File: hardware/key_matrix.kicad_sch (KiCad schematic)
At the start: 90 parts, among them SW10 SW_SPST, SW11 SW_SPST, SW12 SW_SPST, SW13 SW_SPST, SW14 SW_SPST, SW15 SW_SPST, SW16 SW_SPST, SW17 SW_SPST, SW18 SW_SPST, SW19 SW_SPST, SW2 SW_SPST, SW20 SW_SPST, SW21 SW_SPST, SW22 SW_SPST, SW23 SW_SPST, SW24 SW_SPST, SW25 SW_SPST, SW26 SW_SPST, SW27 SW_SPST, SW28 SW_SPST, SW29 SW_SPST, SW3 SW_SPST, SW30 SW_SPST, SW31 SW_SPST, SW32 SW_SPST, SW33 SW_SPST, SW34 SW_SPST, SW35 SW_SPST, SW36 SW_SPST, SW37 SW_SPST, SW38 SW_SPST, SW39 SW_SPST, SW4 SW_SPST, SW40 SW_SPST, SW41 SW_SPST, SW42 SW_SPST, SW43 SW_SPST, SW44 SW_SPST, SW45 SW_SPST, SW46 SW_SPST, SW47 SW_SPST, SW48 SW_SPST, SW49 SW_SPST, SW5 SW_SPST, SW50 SW_SPST, SW51 SW_SPST, SW52 SW_SPST, SW53 SW_SPST, SW54 SW_SPST, SW55 SW_SPST, SW56 SW_SPST, SW57 SW_SPST, SW58 SW_SPST, SW59 SW_SPST, SW6 SW_SPST, SW60 SW_SPST, SW61 SW_SPST, SW62 SW_SPST, SW63 SW_SPST, SW64 SW_SPST, SW65 SW_SPST, SW66 SW_SPST, SW67 SW_SPST, SW68 SW_SPST, SW69 SW_SPST, SW7 SW_SPST, SW70 SW_SPST, SW71 SW_SPST, SW72 SW_SPST, SW73 SW_SPST, SW75 SW_SPST, SW76 SW_SPST, SW77 SW_SPST, SW78 SW_SPST, SW79 SW_SPST, SW8 SW_SPST, SW80 SW_SPST, SW81 SW_SPST, SW82 SW_SPST, SW9 SW_SPST

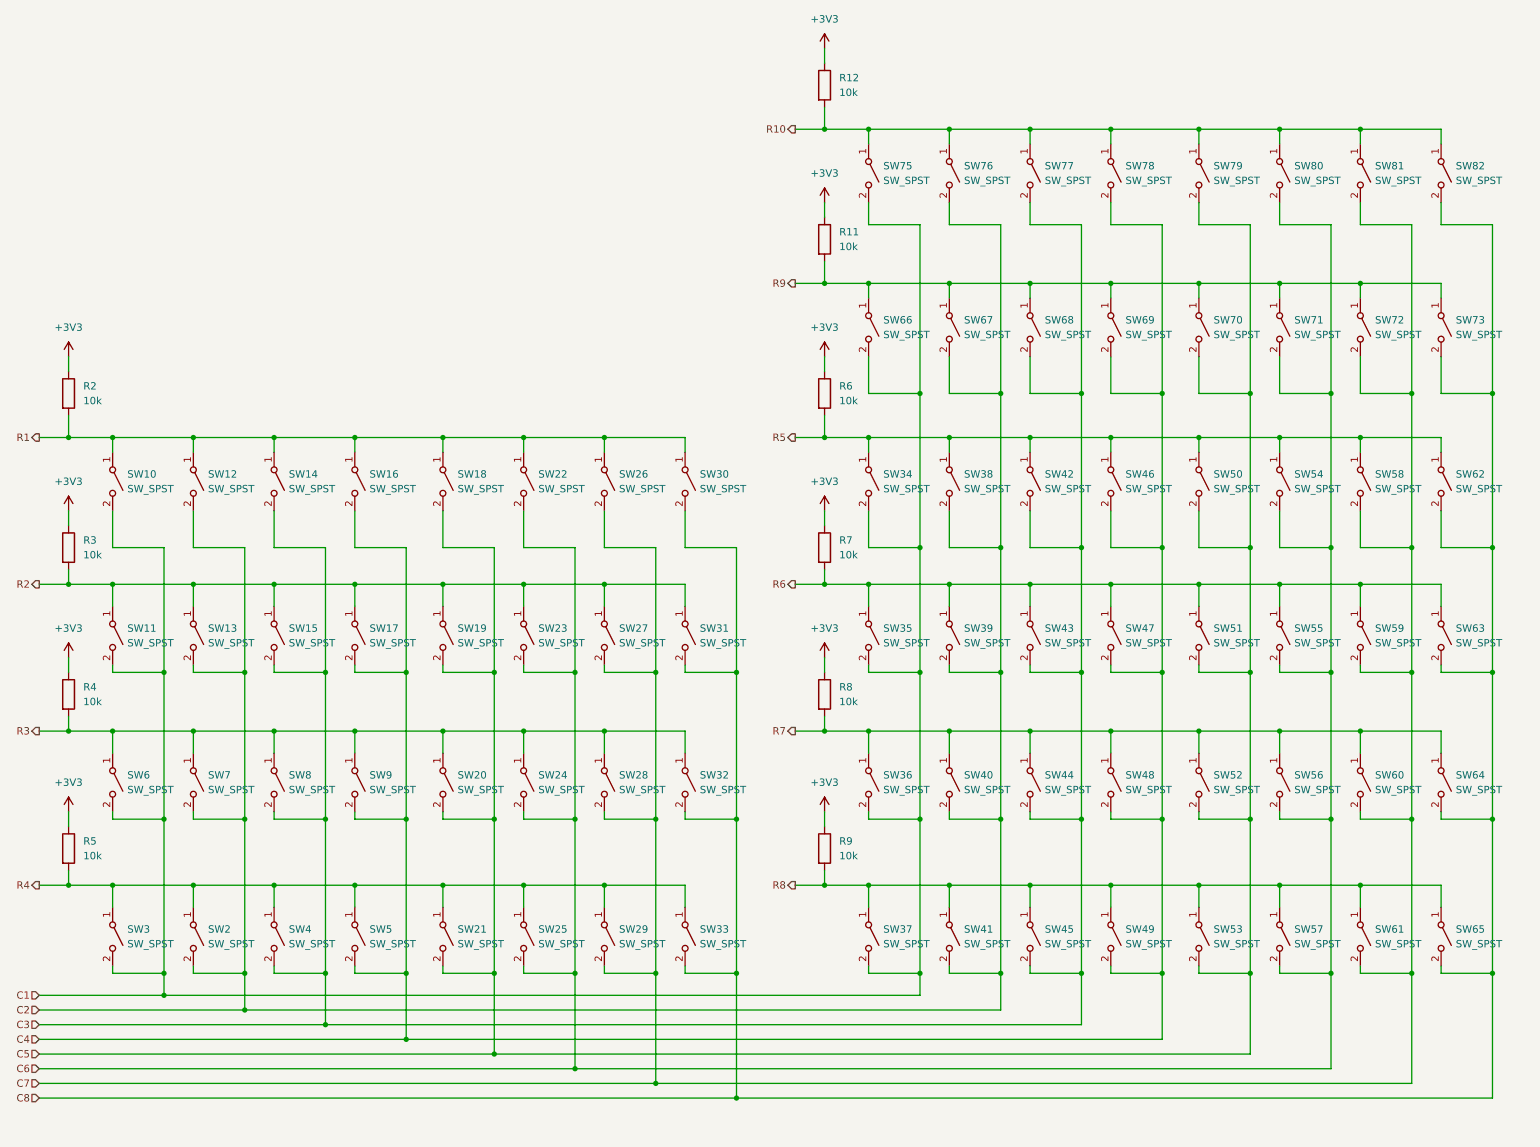
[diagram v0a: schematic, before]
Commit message: Add diodes to schematic to prevent ghosting
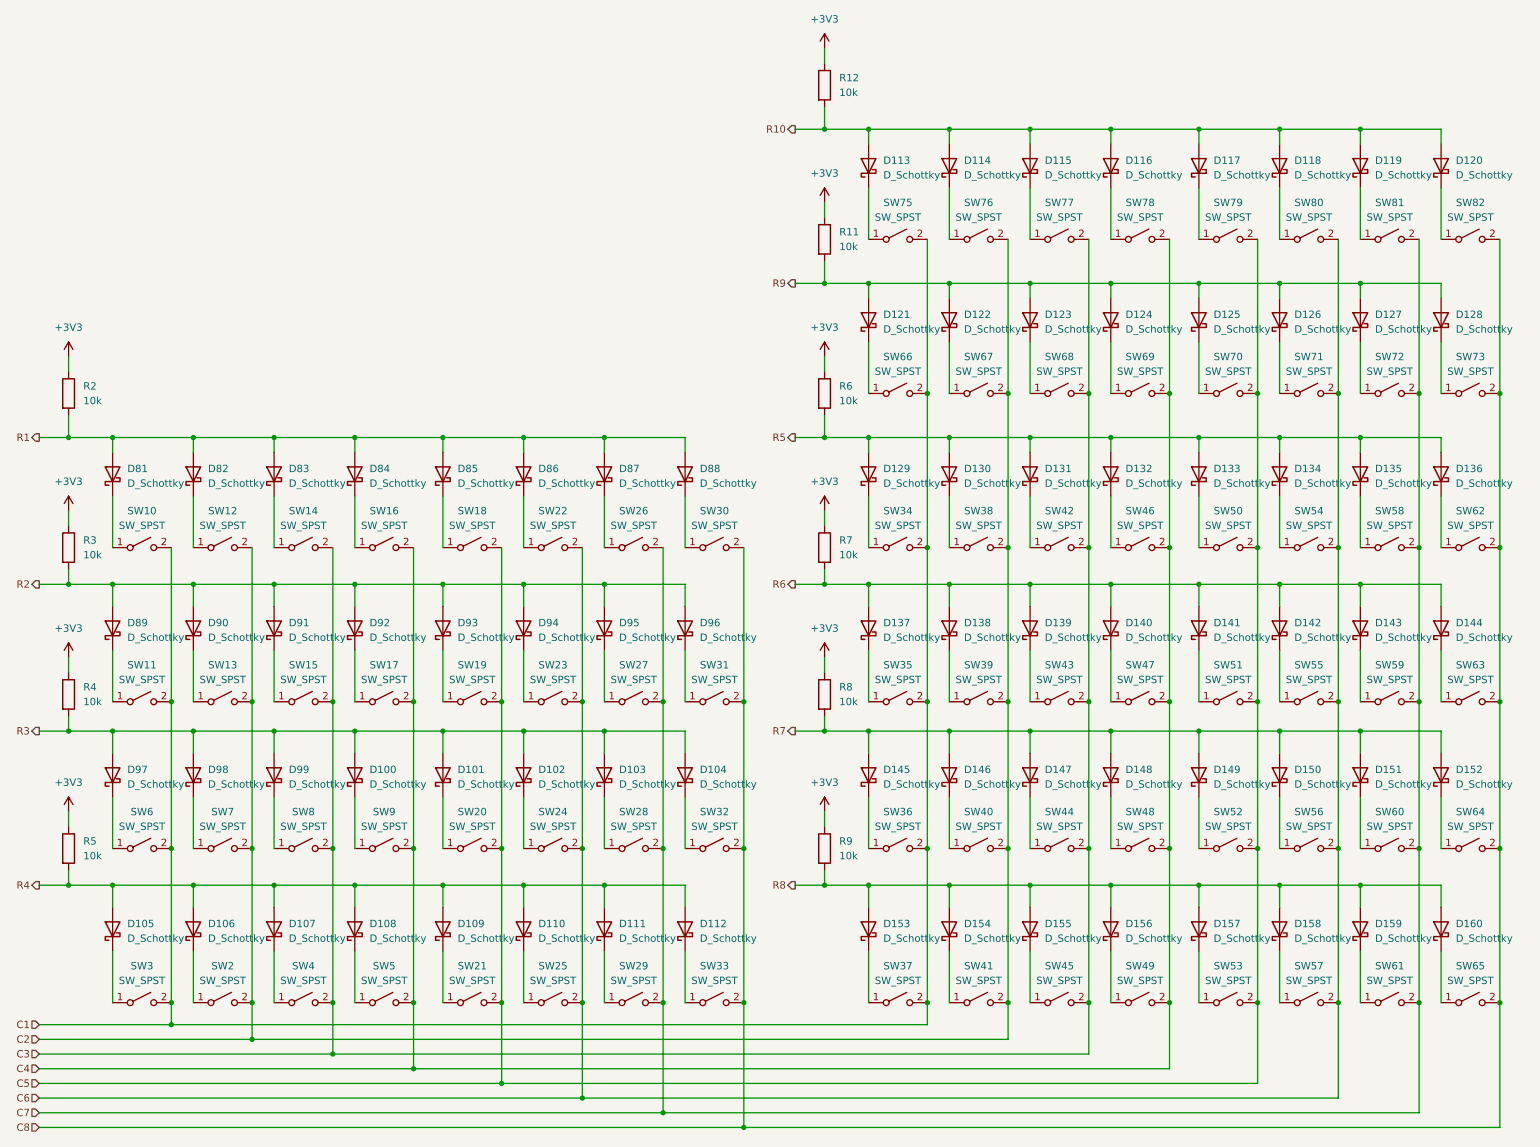
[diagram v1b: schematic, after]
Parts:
- added D100, D101, D102, D103, D104, D105, D106, D107, D108, D109, D110, D111, D112, D113, D114, D115, D116, D117, D118, D119, D120, D121, D122, D123, D124, D125, D126, D127, D128, D129, D130, D131, D132, D133, D134, D135, D136, D137, D138, D139, D140, D141, D142, D143, D144, D145, D146, D147, D148, D149, D150, D151, D152, D153, D154, D155, D156, D157, D158, D159, D160, D81, D82, D83, D84, D85, D86, D87, D88, D89, D90, D91, D92, D93, D94, D95, D96, D97, D98, D99: D_Schottky, Diode_SMD:D_SOD-323_HandSoldering, symbol Device:D_Schottky
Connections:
- net R1: now also D81.2 (A), D82.2 (A), D83.2 (A), D84.2 (A), D85.2 (A), D86.2 (A), D87.2 (A), D88.2 (A); no longer SW10.1 (A), SW12.1 (A), SW14.1 (A), SW16.1 (A), SW18.1 (A), SW22.1 (A), SW26.1 (A), SW30.1 (A)
- net R10: now also D113.2 (A), D114.2 (A), D115.2 (A), D116.2 (A), D117.2 (A), D118.2 (A), D119.2 (A), D120.2 (A); no longer SW75.1 (A), SW76.1 (A), SW77.1 (A), SW78.1 (A), SW79.1 (A), SW80.1 (A), SW81.1 (A), SW82.1 (A)
- net R2: now also D89.2 (A), D90.2 (A), D91.2 (A), D92.2 (A), D93.2 (A), D94.2 (A), D95.2 (A), D96.2 (A); no longer SW11.1 (A), SW13.1 (A), SW15.1 (A), SW17.1 (A), SW19.1 (A), SW23.1 (A), SW27.1 (A), SW31.1 (A)
- net R3: now also D100.2 (A), D101.2 (A), D102.2 (A), D103.2 (A), D104.2 (A), D97.2 (A), D98.2 (A), D99.2 (A); no longer SW20.1 (A), SW24.1 (A), SW28.1 (A), SW32.1 (A), SW6.1 (A), SW7.1 (A), SW8.1 (A), SW9.1 (A)
- net R4: now also D105.2 (A), D106.2 (A), D107.2 (A), D108.2 (A), D109.2 (A), D110.2 (A), D111.2 (A), D112.2 (A); no longer SW2.1 (A), SW21.1 (A), SW25.1 (A), SW29.1 (A), SW3.1 (A), SW33.1 (A), SW4.1 (A), SW5.1 (A)
- net R5: now also D129.2 (A), D130.2 (A), D131.2 (A), D132.2 (A), D133.2 (A), D134.2 (A), D135.2 (A), D136.2 (A); no longer SW34.1 (A), SW38.1 (A), SW42.1 (A), SW46.1 (A), SW50.1 (A), SW54.1 (A), SW58.1 (A), SW62.1 (A)
- net R6: now also D137.2 (A), D138.2 (A), D139.2 (A), D140.2 (A), D141.2 (A), D142.2 (A), D143.2 (A), D144.2 (A); no longer SW35.1 (A), SW39.1 (A), SW43.1 (A), SW47.1 (A), SW51.1 (A), SW55.1 (A), SW59.1 (A), SW63.1 (A)
- net R7: now also D145.2 (A), D146.2 (A), D147.2 (A), D148.2 (A), D149.2 (A), D150.2 (A), D151.2 (A), D152.2 (A); no longer SW36.1 (A), SW40.1 (A), SW44.1 (A), SW48.1 (A), SW52.1 (A), SW56.1 (A), SW60.1 (A), SW64.1 (A)
- net R8: now also D153.2 (A), D154.2 (A), D155.2 (A), D156.2 (A), D157.2 (A), D158.2 (A), D159.2 (A), D160.2 (A); no longer SW37.1 (A), SW41.1 (A), SW45.1 (A), SW49.1 (A), SW53.1 (A), SW57.1 (A), SW61.1 (A), SW65.1 (A)
- net R9: now also D121.2 (A), D122.2 (A), D123.2 (A), D124.2 (A), D125.2 (A), D126.2 (A), D127.2 (A), D128.2 (A); no longer SW66.1 (A), SW67.1 (A), SW68.1 (A), SW69.1 (A), SW70.1 (A), SW71.1 (A), SW72.1 (A), SW73.1 (A)
- new net: D110.1 (K), SW25.1 (A)
- new net: D149.1 (K), SW52.1 (A)
- new net: D125.1 (K), SW70.1 (A)
- new net: D140.1 (K), SW47.1 (A)
- new net: D95.1 (K), SW27.1 (A)
- new net: D113.1 (K), SW75.1 (A)
- new net: D96.1 (K), SW31.1 (A)
- new net: D119.1 (K), SW81.1 (A)
- new net: D148.1 (K), SW48.1 (A)
- new net: D117.1 (K), SW79.1 (A)
- new net: D94.1 (K), SW23.1 (A)
- new net: D145.1 (K), SW36.1 (A)
- new net: D98.1 (K), SW7.1 (A)
- new net: D103.1 (K), SW28.1 (A)
- new net: D102.1 (K), SW24.1 (A)
- new net: D83.1 (K), SW14.1 (A)
- new net: D89.1 (K), SW11.1 (A)
- new net: D141.1 (K), SW51.1 (A)
- new net: D138.1 (K), SW39.1 (A)
- new net: D84.1 (K), SW16.1 (A)
- new net: D97.1 (K), SW6.1 (A)
- new net: D112.1 (K), SW33.1 (A)
- new net: D108.1 (K), SW5.1 (A)
- new net: D130.1 (K), SW38.1 (A)
- new net: D135.1 (K), SW58.1 (A)
- new net: D160.1 (K), SW65.1 (A)
- new net: D122.1 (K), SW67.1 (A)
- new net: D153.1 (K), SW37.1 (A)
- new net: D114.1 (K), SW76.1 (A)
- new net: D111.1 (K), SW29.1 (A)
- new net: D156.1 (K), SW49.1 (A)
- new net: D107.1 (K), SW4.1 (A)
- new net: D131.1 (K), SW42.1 (A)
- new net: D142.1 (K), SW55.1 (A)
- new net: D101.1 (K), SW20.1 (A)
- new net: D92.1 (K), SW17.1 (A)
- new net: D132.1 (K), SW46.1 (A)
- new net: D126.1 (K), SW71.1 (A)
- new net: D106.1 (K), SW2.1 (A)
- new net: D86.1 (K), SW22.1 (A)
- new net: D127.1 (K), SW72.1 (A)
- new net: D87.1 (K), SW26.1 (A)
- new net: D82.1 (K), SW12.1 (A)
- new net: D139.1 (K), SW43.1 (A)
- new net: D155.1 (K), SW45.1 (A)
- new net: D154.1 (K), SW41.1 (A)
- new net: D105.1 (K), SW3.1 (A)
- new net: D129.1 (K), SW34.1 (A)
- new net: D124.1 (K), SW69.1 (A)
- new net: D81.1 (K), SW10.1 (A)
- new net: D93.1 (K), SW19.1 (A)
- new net: D150.1 (K), SW56.1 (A)
- new net: D115.1 (K), SW77.1 (A)
- new net: D91.1 (K), SW15.1 (A)
- new net: D120.1 (K), SW82.1 (A)
- new net: D121.1 (K), SW66.1 (A)
- new net: D123.1 (K), SW68.1 (A)
- new net: D104.1 (K), SW32.1 (A)
- new net: D144.1 (K), SW63.1 (A)
- new net: D152.1 (K), SW64.1 (A)
- new net: D143.1 (K), SW59.1 (A)
- new net: D118.1 (K), SW80.1 (A)
- new net: D90.1 (K), SW13.1 (A)
- new net: D158.1 (K), SW57.1 (A)
- new net: D151.1 (K), SW60.1 (A)
- new net: D109.1 (K), SW21.1 (A)
- new net: D100.1 (K), SW9.1 (A)
- new net: D133.1 (K), SW50.1 (A)
- new net: D99.1 (K), SW8.1 (A)
- new net: D159.1 (K), SW61.1 (A)
- new net: D128.1 (K), SW73.1 (A)
- new net: D88.1 (K), SW30.1 (A)
- new net: D157.1 (K), SW53.1 (A)
- new net: D134.1 (K), SW54.1 (A)
- new net: D85.1 (K), SW18.1 (A)
- new net: D136.1 (K), SW62.1 (A)
- new net: D147.1 (K), SW44.1 (A)
- new net: D146.1 (K), SW40.1 (A)
- new net: D137.1 (K), SW35.1 (A)
- new net: D116.1 (K), SW78.1 (A)
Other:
- moved on the sheet: SW10, SW11, SW12, SW13, SW14, SW15, SW16, SW17, SW18, SW19, SW2, SW20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
